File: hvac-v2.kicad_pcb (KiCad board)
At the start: 2 copper layers, 114 x 59 mm, 35 parts, among them J2 Anderson_two_redblack, J3 Anderson_two_redblack, J4 Anderson_two_redblack, P1 10118194, P2 CONN_01X08, SW1 SW_SPST, SW3 KS-01Q-01, SW4 KS-01Q-01, SW5 SPST, U1 SAMD21E18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

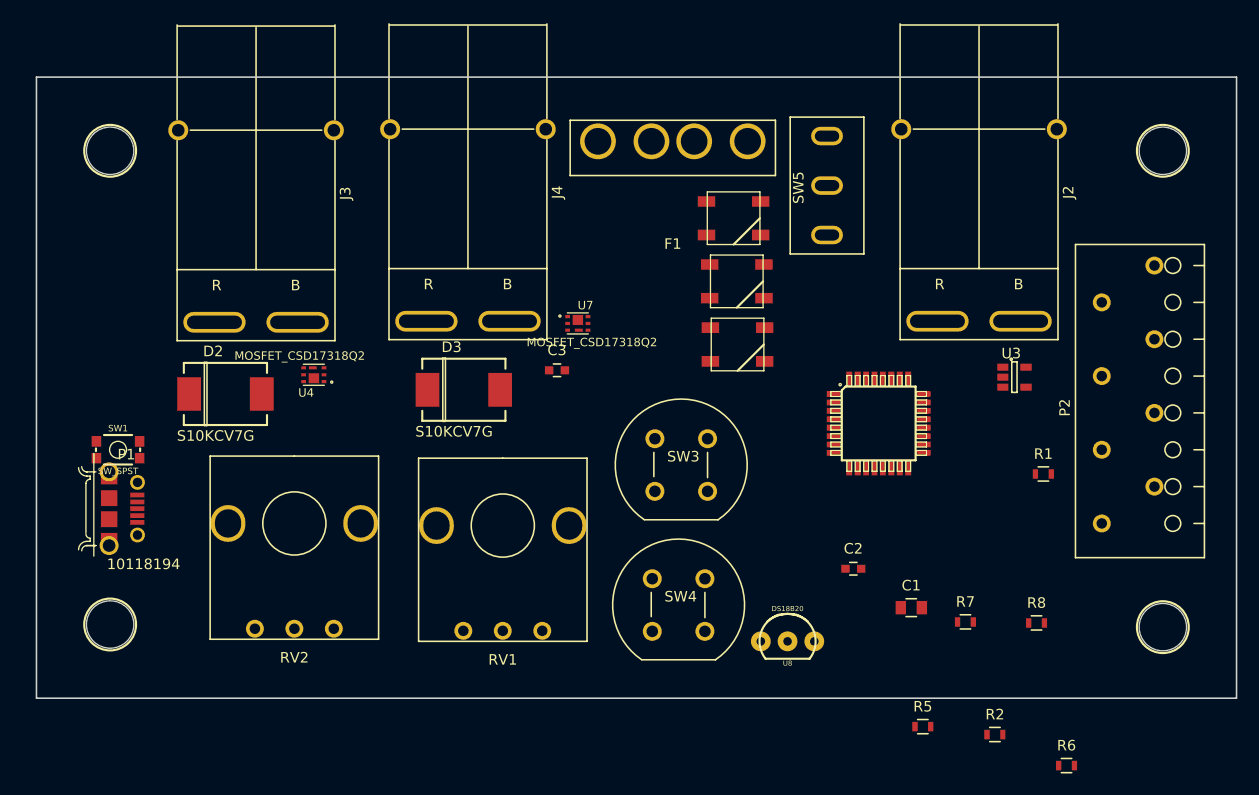
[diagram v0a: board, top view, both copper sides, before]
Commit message: Route power (GIANT TRACES)
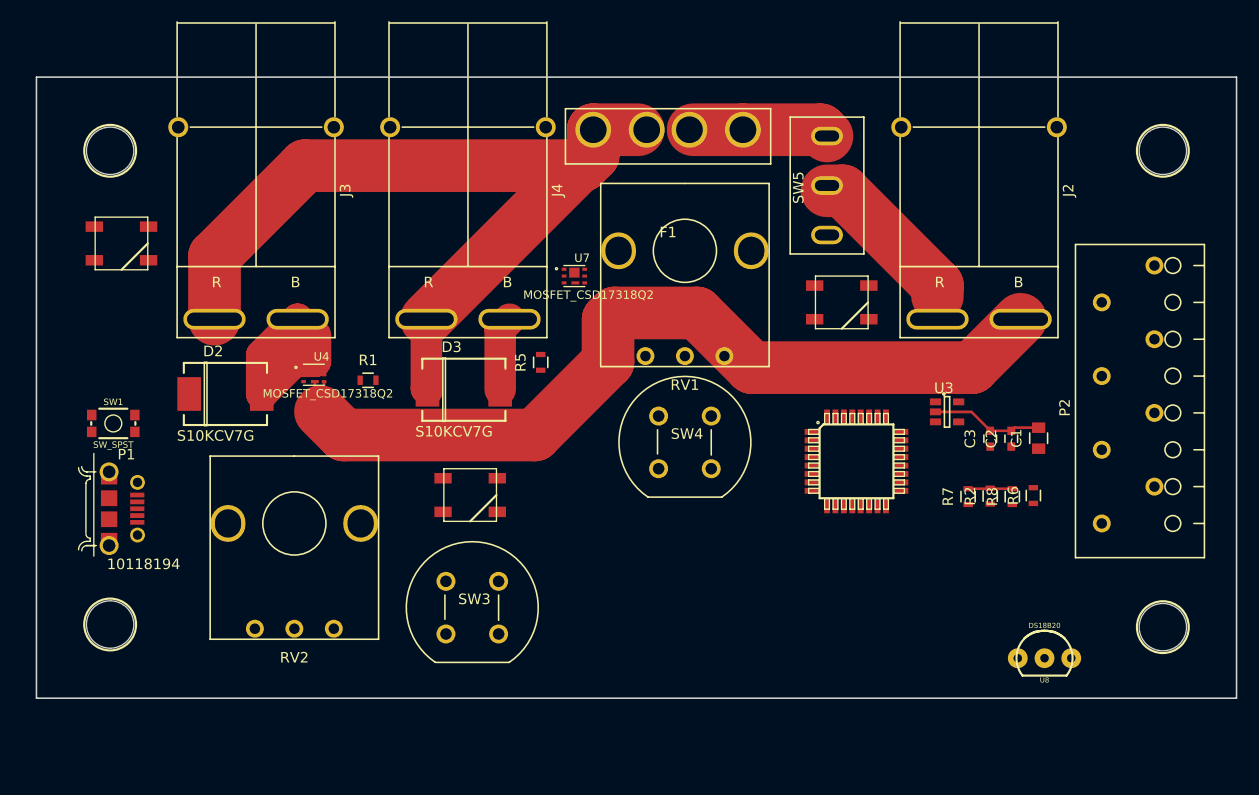
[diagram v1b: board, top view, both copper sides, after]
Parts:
- moved R1 64.8 mm to (77.5, 73.8)
- moved U2 58.6 mm to (54.1, 60.8)
- moved R5 50.1 mm to (93.9, 72.1), turned to 90 degrees
- moved C3 41.7 mm to (136.6, 79.3), turned to 90 degrees
- moved RV1 31.3 mm to (107.6, 71.5)
- moved U6 29.1 mm to (87.2, 84.7)
- moved R6 25.8 mm to (140.7, 84.8), turned to 90 degrees
- moved U8 24.5 mm to (141.8, 100.2)
- moved SW3 24.0 mm to (84.9, 92.9)
- moved R2 22.7 mm to (136.6, 84.8), turned to 90 degrees
- moved C1 20.1 mm to (141.2, 79.3), turned to 90 degrees
- moved C2 19.4 mm to (138.6, 79.3), turned to 90 degrees
- moved SW4 15.5 mm to (105.1, 77.2)
- moved U5 13.0 mm to (122.5, 66.4)
- moved R8 12.2 mm to (138.7, 84.8), turned to 90 degrees
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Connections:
- net KNOB renamed SPEED
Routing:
- net GND: track 0.00 -> 99.6 mm
- net +BATT: track 0.00 -> 89.4 mm
- net Net-(J2-Pad1): track 0.00 -> 30.0 mm
- net FAN_OUT: track 0.00 -> 21.4 mm
- net Net-(F1-Pad1): track 0.00 -> 18.1 mm
- net PUMP_OUT: track 0.00 -> 7.07 mm

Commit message: First pass routing. Still has DRC errors
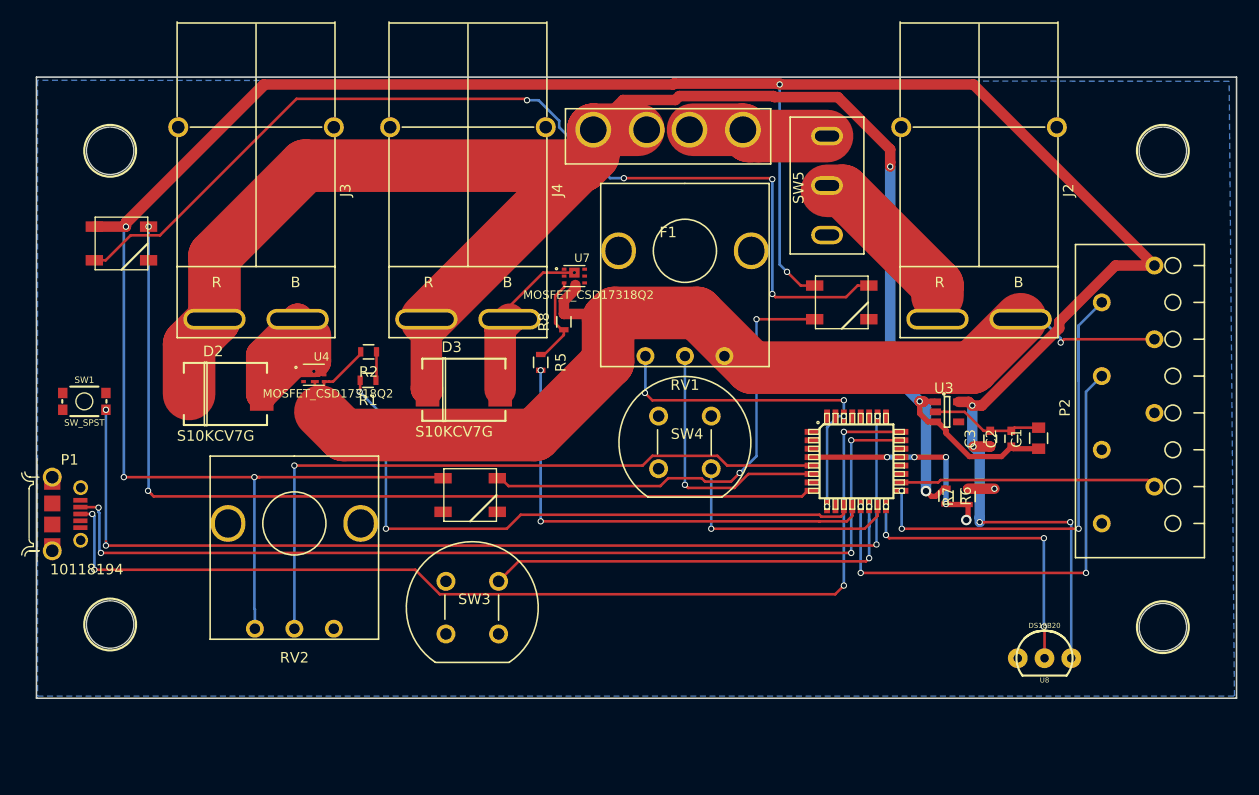
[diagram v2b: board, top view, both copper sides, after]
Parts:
- moved R2 60.6 mm to (77.5, 71.1), turned to 180 degrees
- moved R8 45.7 mm to (96.1, 68.2)
- moved R6 8.30 mm to (132.4, 84.8), turned to 270 degrees
- moved P1 5.42 mm to (47.5, 86.5)
- moved SW1 3.46 mm to (50.5, 75.8)
- turned R1 to 180 degrees
- turned R5 to 270 degrees
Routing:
- net VCC: track 0.00 -> 370.7 mm, vias 0 -> 13
- net USB_D+: track 0.00 -> 99.1 mm, vias 0 -> 4
- net Net-(SW1-Pad2): track 0.00 -> 98.4 mm, vias 0 -> 4
- net Net-(U2-Pad2): track 0.00 -> 94.9 mm, vias 0 -> 4
- net +BATT: track 89.4 -> 183.4 mm, vias 0 -> 3
- net USB_D-: track 0.00 -> 92.9 mm, vias 0 -> 4
- net LED: track 0.00 -> 88.6 mm, vias 0 -> 2
- net MODE: track 0.00 -> 65.4 mm, vias 0 -> 1
- net FAN_SIGNAL: track 0.00 -> 60.1 mm, vias 0 -> 2
- net EXTERNAL_TEMP: track 0.00 -> 48.1 mm, vias 0 -> 3
- net FAN_PWM: track 0.00 -> 47.0 mm, vias 0 -> 3
- net PUMP_SIGNAL: track 0.00 -> 45.1 mm, vias 0 -> 2
- net Net-(U5-Pad2): track 0.00 -> 44.9 mm, vias 0 -> 2
- net NAP_BUTTON: track 0.00 -> 41.7 mm, vias 0 -> 2
- net INTERNAL_TEMP: track 0.00 -> 29.3 mm, vias 0 -> 4
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- added copper zone on B.Cu, net GND

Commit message: DRC fixes
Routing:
- net GND: track 126.6 -> 154.3 mm, vias 2 -> 3
- net Net-(R1-Pad1): track 2.72 -> 12.1 mm, vias 0 -> 2
- net VCC: track 370.7 -> 376.8 mm, vias 13 -> 14
- net NAP_BUTTON: track 41.7 -> 46.7 mm
- net AUX_BUTTON: track 22.9 -> 27.9 mm
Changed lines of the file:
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@@
   (general
     (links 90)
-    (no_connects 23)
+    (no_connects 20)
     (area 45.924999 44.924999 160.075001 104.075001)
     (thickness 1.6)
     (drawings 4)
-    (tracks 377)
+    (tracks 391)
     (zones 0)
     (modules 35)
@@
   )
   (setup
-    (last_trace_width 0.5)
+    (last_trace_width 0.25)
     (user_trace_width 0.25)
     (user_trace_width 0.5)
@@
   (gr_line (start 160 45) (end 160 104) (layer Edge.Cuts) (width 0.15))
   (gr_line (start 46 45) (end 160 45) (layer Edge.Cuts) (width 0.15))
-  (segment (start 52.59956 89.09956) (end 52.6 89.1) (width 0.25) (layer F.Cu) (net 0))
   (segment (start 131.426001 84.823999) (end 130.999999 84.823999) (width 0.5) (layer F.Cu) (net 1))
   (segment (start 130.999999 84.823999) (end 130.5 84.324) (width 0.5) (layer F.Cu) (net 1))
@@
   (segment (start 129.9 76.224264) (end 129.9 75.8) (width 0.5) (layer F.Cu) (net 1))
   (segment (start 129.9 75.8) (end 131.35 75.8) (width 0.5) (layer F.Cu) (net 1))
-  (segment (start 131.35 75.8) (end 131.4 75.85) (width 0.5) (layer F.Cu) (net 1))
   (segment (start 129.9 75.8) (end 130.284998 75.8) (width 1) (layer F.Cu) (net 1))
-  (segment (start 129.9 75.8) (end 129.95 75.85) (width 1) (layer F.Cu) (net 1))
   (segment (start 129.95 75.85) (end 130.234998 75.85) (width 1) (layer F.Cu) (net 1))
   (segment (start 127.1 53.5) (end 127.1 73) (width 1) (layer B.Cu) (net 1))
@@
   (segment (start 83.04 74.59) (end 83.15 74.7) (width 3) (layer F.Cu) (net 1))
   (segment (start 103.97 50) (end 98.89 50) (width 3) (layer F.Cu) (net 1))
+  (segment (start 134.89 72.6) (end 125 72.6) (width 5) (layer F.Cu) (net 2))
+  (segment (start 125 72.6) (end 113.954002 72.6) (width 5) (layer F.Cu) (net 2))
+  (segment (start 125.07556 67.99766) (end 125.07556 72.52444) (width 1) (layer F.Cu) (net 2))
+  (segment (start 125.07556 72.52444) (end 125 72.6) (width 1) (layer F.Cu) (net 2))
+  (via (at 106.049999 67.650001) (size 0.6) (drill 0.4) (layers F.Cu B.Cu) (net 2))
+  (segment (start 105.1 77.2) (end 105.1 75.927208) (width 1) (layer B.Cu) (net 2))
+  (segment (start 105.1 75.927208) (end 106.049999 74.977209) (width 1) (layer B.Cu) (net 2))
+  (segment (start 106.049999 74.977209) (end 106.049999 67.650001) (width 1) (layer B.Cu) (net 2))
+  (segment (start 105.1 77.2) (end 105.1 82.2) (width 1) (layer B.Cu) (net 2))
+  (segment (start 143.296276 69.826276) (end 152.126276 69.826276) (width 1) (layer F.Cu) (net 2))
+  (segment (start 152.126276 69.826276) (end 152.2 69.9) (width 1) (layer F.Cu) (net 2))
+  (segment (start 139.49 68) (end 141.47 68) (width 1) (layer B.Cu) (net 2))
+  (segment (start 141.47 68) (end 143.296276 69.826276) (width 1) (layer B.Cu) (net 2))
+  (via (at 143.296276 69.826276) (size 0.6) (drill 0.4) (layers F.Cu B.Cu) (net 2))
   (segment (start 134.175 76.8) (end 132.18 76.8) (width 0.25) (layer F.Cu) (net 2))
   (segment (start 135.975 78.6) (end 134.175 76.8) (width 0.25) (layer F.Cu) (net 2))
@@
   (segment (start 134.5 84.1) (end 137 84.1) (width 1) (layer F.Cu) (net 2))
   (via (at 137 84.1) (size 0.6) (drill 0.4) (layers F.Cu B.Cu) (net 2))
-  (segment (start 143.596275 69.917967) (end 143.296276 70.217966) (width 0.25) (layer F.Cu) (net 2))
   (segment (start 143.614242 69.9) (end 143.596275 69.917967) (width 0.25) (layer F.Cu) (net 2))
-  (segment (start 141.47 68) (end 143.296276 69.826276) (width 0.25) (layer B.Cu) (net 2))
-  (segment (start 139.49 68) (end 141.47 68) (width 0.25) (layer B.Cu) (net 2))
   (segment (start 152.2 69.9) (end 143.614242 69.9) (width 0.25) (layer F.Cu) (net 2))
-  (segment (start 143.296276 69.826276) (end 143.296276 70.217966) (width 0.25) (layer B.Cu) (net 2))
-  (via (at 143.296276 70.217966) (size 0.6) (drill 0.4) (layers F.Cu B.Cu) (net 2))
   (segment (start 96.1 67.5) (end 96.1 66.25) (width 1) (layer F.Cu) (net 2))
   (segment (start 96.1 66.25) (end 97.195 65.155) (width 1) (layer F.Cu) (net 2))
@@
   (segment (start 108.754002 67.4) (end 100.925001 67.4) (width 5) (layer F.Cu) (net 2))
   (segment (start 139.49 68) (end 134.89 72.6) (width 5) (layer F.Cu) (net 2))
-  (segment (start 134.89 72.6) (end 113.954002 72.6) (width 5) (layer F.Cu) (net 2))
   (segment (start 113.954002 72.6) (end 108.754002 67.4) (width 5) (layer F.Cu) (net 2))
-  (segment (start 134.9 76.2) (end 134.9 79.984312) (width 1) (layer B.Cu) (net 3))
+  (segment (start 135 76.2) (end 149.8 76.2) (width 1) (layer F.Cu) (net 3))
+  (segment (start 149.8 76.2) (end 150.2 75.8) (width 1) (layer F.Cu) (net 3))
+  (segment (start 135 76.2) (end 135 80.084312) (width 1) (layer B.Cu) (net 3))
+  (segment (start 135 80.084312) (end 135.007844 80.092156) (width 1) (layer B.Cu) (net 3))
+  (segment (start 133.6 75.85) (end 134.65 75.85) (width 1) (layer F.Cu) (net 3))
+  (segment (start 134.65 75.85) (end 135 76.2) (width 1) (layer F.Cu) (net 3))
+  (via (at 135 76.2) (size 0.6) (drill 0.4) (layers F.Cu B.Cu) (net 3))
+  (segment (start 152.2 62.9) (end 150.2 64.9) (width 1) (layer B.Cu) (net 3))
+  (segment (start 150.2 64.9) (end 150.2 75.8) (width 1) (layer B.Cu) (net 3))
+  (via (at 150.2 75.8) (size 0.6) (drill 0.4) (layers F.Cu B.Cu) (net 3))
   (segment (start 134.9 79.984312) (end 135.007844 80.092156) (width 1) (layer B.Cu) (net 3))
-  (segment (start 134.9 76.2) (end 135.815496 76.2) (width 1) (layer F.Cu) (net 3))
-  (segment (start 135.815496 76.2) (end 143.15501 68.860486) (width 1) (layer F.Cu) (net 3))
-  (segment (start 143.15501 68.860486) (end 143.15501 68.24499) (width 1) (layer F.Cu) (net 3))
-  (segment (start 143.15501 68.24499) (end 148.5 62.9) (width 1) (layer F.Cu) (net 3))
-  (segment (start 148.5 62.9) (end 152.2 62.9) (width 1) (layer F.Cu) (net 3))
-  (segment (start 133.6 75.85) (end 134.55 75.85) (width 1) (layer F.Cu) (net 3))
-  (segment (start 134.55 75.85) (end 134.9 76.2) (width 1) (layer F.Cu) (net 3))
   (segment (start 136.024264 87.27498) (end 144.2 87.27498) (width 0.25) (layer F.Cu) (net 3))
   (segment (start 135.6 87.27498) (end 136.024264 87.27498) (width 0.25) (layer F.Cu) (net 3))
@@
   (segment (start 122.37498 45.97498) (end 120.87498 45.97498) (width 0.25) (layer F.Cu) (net 3))
   (via (at 135.007844 80.092156) (size 0.6) (drill 0.4) (layers F.Cu B.Cu) (net 3))
-  (via (at 134.9 76.2) (size 0.6) (drill 0.4) (layers F.Cu B.Cu) (net 3))
   (segment (start 72.5 72) (end 72.5 69.5) (width 3) (layer F.Cu) (net 4))
   (segment (start 67.4 75.1) (end 70.515 71.985) (width 3) (layer F.Cu) (net 4))
@@
   (segment (start 131.666018 83.49898) (end 131.890008 83.27499) (width 0.25) (layer F.Cu) (net 15))
   (segment (start 131.890008 83.27499) (end 151.57499 83.27499) (width 0.25) (layer F.Cu) (net 15))
+  (segment (start 70.6 74.9) (end 71.7 73.8) (width 0.25) (layer B.Cu) (net 17))
+  (segment (start 71.7 73.8) (end 78.25 73.8) (width 0.25) (layer B.Cu) (net 17))
+  (via (at 78.25 73.8) (size 0.6) (drill 0.4) (layers F.Cu B.Cu) (net 17))
+  (segment (start 71.375 73.925) (end 71.375 74.125) (width 0.25) (layer F.Cu) (net 17))
+  (segment (start 71.375 74.125) (end 70.6 74.9) (width 0.25) (layer F.Cu) (net 17))
+  (via (at 70.6 74.9) (size 0.6) (drill 0.4) (layers F.Cu B.Cu) (net 17))
   (segment (start 78.3 71.1) (end 78.3 73.75) (width 0.25) (layer F.Cu) (net 17))
   (segment (start 78.3 73.75) (end 78.25 73.8) (width 0.25) (layer F.Cu) (net 17))
@@
   (segment (start 103.586998 81.9) (end 70.5 81.9) (width 0.25) (layer F.Cu) (net 22))
   (via (at 70.5 81.9) (size 0.6) (drill 0.4) (layers F.Cu B.Cu) (net 22))
+  (segment (start 53.1 89.5) (end 125.7 89.5) (width 0.25) (layer F.Cu) (net 23))
+  (segment (start 125.7 89.5) (end 125.8 89.4) (width 0.25) (layer F.Cu) (net 23))
+  (segment (start 53.1 89.5) (end 53.1 77.10044) (width 0.25) (layer B.Cu) (net 23))
+  (segment (start 53.1 77.10044) (end 52.59956 76.6) (width 0.25) (layer B.Cu) (net 23))
   (segment (start 125.8 89.4) (end 125.8 77.30638) (width 0.25) (layer B.Cu) (net 23))
   (segment (start 125.8 77.30638) (end 125.89898 77.2074) (width 0.25) (layer B.Cu) (net 23))
   (via (at 125.89898 77.2074) (size 0.6) (drill 0.4) (layers F.Cu B.Cu) (net 23))
-  (segment (start 52.6 89.5) (end 125.7 89.5) (width 0.25) (layer F.Cu) (net 23))
-  (segment (start 125.7 89.5) (end 125.8 89.4) (width 0.25) (layer F.Cu) (net 23))
   (via (at 125.8 89.4) (size 0.6) (drill 0.4) (layers F.Cu B.Cu) (net 23))
-  (segment (start 52.59956 76.6) (end 52.59956 89.49956) (width 0.25) (layer B.Cu) (net 23))
-  (segment (start 52.59956 89.49956) (end 52.6 89.5) (width 0.25) (layer B.Cu) (net 23))
-  (via (at 52.6 89.5) (size 0.6) (drill 0.4) (layers F.Cu B.Cu) (net 23))
+  (via (at 53.1 89.5) (size 0.6) (drill 0.4) (layers F.Cu B.Cu) (net 23))
   (via (at 52.59956 76.6) (size 0.6) (drill 0.4) (layers F.Cu B.Cu) (net 23))
+  (segment (start 89.9 92.9) (end 89.9 97.9) (width 1) (layer B.Cu) (net 24))
   (segment (start 90.799999 92.000001) (end 89.9 92.9) (width 0.25) (layer F.Cu) (net 24))
   (segment (start 91.800001 90.999999) (end 90.799999 92.000001) (width 0.25) (layer F.Cu) (net 24))
@@
   (segment (start 125.1 85.79372) (end 125.09888 85.7926) (width 0.25) (layer F.Cu) (net 24))
   (via (at 125.1 90.7) (size 0.6) (drill 0.4) (layers F.Cu B.Cu) (net 24))
+  (segment (start 110.1 77.2) (end 110.1 82.2) (width 1) (layer B.Cu) (net 25))
   (segment (start 110.1 87.9) (end 110.1 82.2) (width 0.25) (layer B.Cu) (net 25))
   (segment (start 125.89898 85.7926) (end 125.89898 86.6776) (width 0.25) (layer F.Cu) (net 25))

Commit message: More DRC fixes
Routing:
- net GND: track 154.3 -> 301.6 mm, vias 3 -> 16
- net Net-(J2-Pad1): track 30.0 -> 47.5 mm
- net VCC: track 376.8 -> 391.0 mm, vias 14 -> 15
- net PUMP_OUT: track 15.8 -> 24.6 mm
- net FAN_OUT: track 21.4 -> 27.1 mm
- net USB_D+: track 99.1 -> 98.5 mm

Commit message: Move cut line up by a mm
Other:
- board size 114 x 59 mm -> 114 x 60 mm
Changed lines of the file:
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@@
   (general
     (links 90)
-    (no_connects 1)
+    (no_connects 0)
     (area 45.924999 44.924999 160.075001 104.075001)
     (thickness 1.6)
@@
       (net 4 FAN_OUT))
   )
-  (gr_line (start 46 104) (end 46 45) (layer Edge.Cuts) (width 0.15))
+  (gr_line (start 46 104) (end 46 44) (layer Edge.Cuts) (width 0.15))
   (gr_line (start 160 104) (end 46 104) (layer Edge.Cuts) (width 0.15))
-  (gr_line (start 160 45) (end 160 104) (layer Edge.Cuts) (width 0.15))
-  (gr_line (start 46 45) (end 160 45) (layer Edge.Cuts) (width 0.15))
+  (gr_line (start 160 44) (end 160 104) (layer Edge.Cuts) (width 0.15))
+  (gr_line (start 46 44) (end 160 44) (layer Edge.Cuts) (width 0.15))
   (segment (start 129.9 76.886812) (end 129.9 76.224264) (width 0.5) (layer F.Cu) (net 1))
   (segment (start 129.9 76.224264) (end 129.9 75.8) (width 0.5) (layer F.Cu) (net 1))
